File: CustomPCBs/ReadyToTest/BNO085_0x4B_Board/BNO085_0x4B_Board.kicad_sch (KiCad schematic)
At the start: 12 parts, among them J1 Conn_01x04_Pin, Y1 32.768kHz

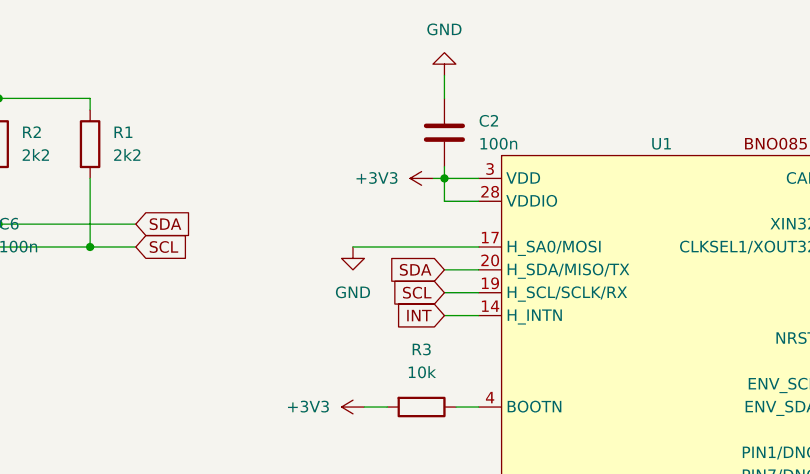
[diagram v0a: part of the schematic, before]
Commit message: Updating IMU boards for different wire connections
Now all components are placed on one layer, making assembly easier. The
JST connector was dropped for smalled IMU housing, instead the wires now
solder directly to the board and exit from the sides of the board.
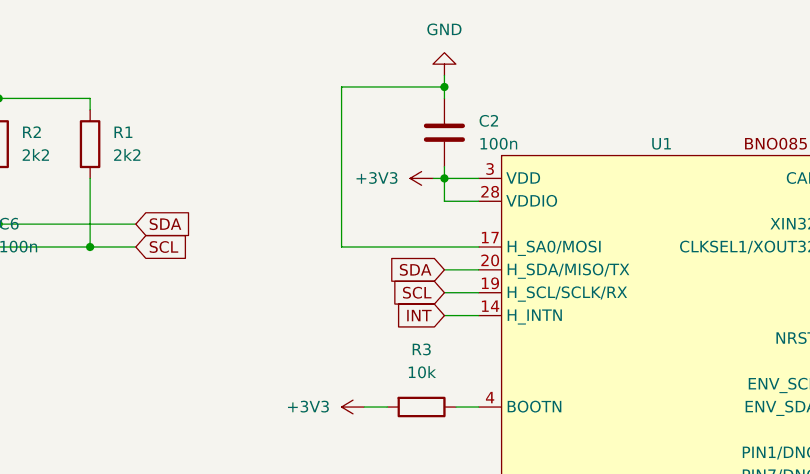
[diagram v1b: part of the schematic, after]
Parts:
- J1: footprint Connector_JST:JST_SH_SM04B-SRSS-TB_1x04-1MP_P1.00mm_Horizontal -> Library:WireToBoard2x2Wide
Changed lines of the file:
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@@
   (junction (at 40.64 38.1) (diameter 0) (color 0 0 0 0)
   )
+  (junction (at 90.17 22.86) (diameter 0) (color 0 0 0 0)
+  )
   (junction (at 173.99 40.64) (diameter 0) (color 0 0 0 0)
   )
@@
   (junction (at 158.75 40.64) (diameter 0) (color 0 0 0 0)
   )
-  (wire (pts (xy 80.01 40.64) (xy 93.98 40.64))
-    (stroke (width 0) (type default))
-  )
   (wire (pts (xy 90.17 73.66) (xy 93.98 73.66))
     (stroke (width 0) (type default))
@@
     (stroke (width 0) (type default))
   )
+  (wire (pts (xy 78.74 22.86) (xy 90.17 22.86))
+    (stroke (width 0) (type default))
+  )
   (wire (pts (xy 50.8 40.64) (xy 30.48 40.64))
     (stroke (width 0) (type default))
@@
     (stroke (width 0) (type default))
   )
+  (wire (pts (xy 78.74 40.64) (xy 93.98 40.64))
+    (stroke (width 0) (type default))
+  )
   (wire (pts (xy 173.99 40.64) (xy 173.99 41.91))
     (stroke (width 0) (type default))
   )
+  (wire (pts (xy 78.74 40.64) (xy 78.74 22.86))
+    (stroke (width 0) (type default))
+  )
   (wire (pts (xy 166.37 50.8) (xy 173.99 50.8))
     (stroke (width 0) (type default))
@@
     (stroke (width 0) (type default))
   )
+  (wire (pts (xy 90.17 22.86) (xy 90.17 24.13))
+    (stroke (width 0) (type default))
+  )
   (wire (pts (xy 90.17 81.28) (xy 90.17 83.82))
     (stroke (width 0) (type default))
@@
     (stroke (width 0) (type default))
   )
-  (wire (pts (xy 90.17 21.59) (xy 90.17 24.13))
+  (wire (pts (xy 90.17 21.59) (xy 90.17 22.86))
     (stroke (width 0) (type default))
   )
@@
     )
   )
-  (symbol (lib_id "power:GND") (at 80.01 40.64 0) (unit 1)
-    (in_bom yes) (on_board yes) (dnp no) (fields_autoplaced)
-    (property "Reference" "#PWR04" (at 80.01 46.99 0)
-      (effects (font (size 1.27 1.27)) hide)
-    )
-    (property "Value" "GND" (at 80.01 45.72 0)
-      (effects (font (size 1.27 1.27)))
-    )
-    (property "Footprint" "" (at 80.01 40.64 0)
-      (effects (font (size 1.27 1.27)) hide)
-    )
-    (property "Datasheet" "" (at 80.01 40.64 0)
-      (effects (font (size 1.27 1.27)) hide)
-    )
-    (pin "1")
-    (instances
-      (project "BNO085_0x4A_Board"
-        (path "/70e5a8fd-d79a-42f0-963c-2c04abcfaf88"
-          (reference "#PWR04") (unit 1)
-        )
-      )
-    )
-  )
   (symbol (lib_id "Device:R") (at 140.97 50.8 270) (unit 1)
     (in_bom yes) (on_board yes) (dnp no) (fields_autoplaced)
@@
     (pin "2")
     (instances
-      (project "BNO085_0x4A_Board"
+      (project "BNO085_0x4B_Board"
         (path "/70e5a8fd-d79a-42f0-963c-2c04abcfaf88"
           (reference "R4") (unit 1)
@@
     (pin "2")
     (instances
-      (project "BNO085_0x4A_Board"
+      (project "BNO085_0x4B_Board"
         (path "/70e5a8fd-d79a-42f0-963c-2c04abcfaf88"
           (reference "R1") (unit 1)
@@
     (pin "2")
     (instances
-      (project "BNO085_0x4A_Board"
+      (project "BNO085_0x4B_Board"
         (path "/70e5a8fd-d79a-42f0-963c-2c04abcfaf88"
           (reference "C6") (unit 1)
@@
     (pin "2")
     (instances
-      (project "BNO085_0x4A_Board"
+      (project "BNO085_0x4B_Board"
         (path "/70e5a8fd-d79a-42f0-963c-2c04abcfaf88"
           (reference "C1") (unit 1)
@@
     (pin "1")
     (instances
-      (project "BNO085_0x4A_Board"
+      (project "BNO085_0x4B_Board"
         (path "/70e5a8fd-d79a-42f0-963c-2c04abcfaf88"
           (reference "#PWR02") (unit 1)
@@
     (pin "1")
     (instances
-      (project "BNO085_0x4A_Board"
+      (project "BNO085_0x4B_Board"
         (path "/70e5a8fd-d79a-42f0-963c-2c04abcfaf88"
           (reference "#PWR011") (unit 1)
@@
     (pin "2")
     (instances
-      (project "BNO085_0x4A_Board"
+      (project "BNO085_0x4B_Board"
         (path "/70e5a8fd-d79a-42f0-963c-2c04abcfaf88"
           (reference "C5") (unit 1)
@@
       (effects (font (size 1.27 1.27)))
     )
-    (property "Footprint" "Connector_JST:JST_SH_SM04B-SRSS-TB_1x04-1MP_P1.00mm_Horizontal" (at 25.4 38.1 0)
+    (property "Footprint" "Library:WireToBoard2x2Wide" (at 25.4 38.1 0)
       (effects (font (size 1.27 1.27)) hide)
     )
@@
     (pin "4")
     (instances
-      (project "BNO085_0x4A_Board"
+      (project "BNO085_0x4B_Board"
         (path "/70e5a8fd-d79a-42f0-963c-2c04abcfaf88"
           (reference "J1") (unit 1)
@@
     (pin "9")
     (instances
-      (project "BNO085_0x4A_Board"
+      (project "BNO085_0x4B_Board"
         (path "/70e5a8fd-d79a-42f0-963c-2c04abcfaf88"
           (reference "U1") (unit 1)
@@
     (pin "1")
     (instances
-      (project "BNO085_0x4A_Board"
+      (project "BNO085_0x4B_Board"
         (path "/70e5a8fd-d79a-42f0-963c-2c04abcfaf88"
           (reference "#PWR06") (unit 1)
@@
     (pin "1")
     (instances
-      (project "BNO085_0x4A_Board"
+      (project "BNO085_0x4B_Board"
         (path "/70e5a8fd-d79a-42f0-963c-2c04abcfaf88"
           (reference "#PWR08") (unit 1)
@@
     (pin "2")
     (instances
-      (project "BNO085_0x4A_Board"
+      (project "BNO085_0x4B_Board"
         (path "/70e5a8fd-d79a-42f0-963c-2c04abcfaf88"
           (reference "C4") (unit 1)
@@
     (pin "2")
     (instances
-      (project "BNO085_0x4A_Board"
+      (project "BNO085_0x4B_Board"
         (path "/70e5a8fd-d79a-42f0-963c-2c04abcfaf88"
           (reference "Y1") (unit 1)
@@
     (pin "1")
     (instances
-      (project "BNO085_0x4A_Board"
+      (project "BNO085_0x4B_Board"
         (path "/70e5a8fd-d79a-42f0-963c-2c04abcfaf88"
           (reference "#PWR03") (unit 1)
@@
     (pin "1")
     (instances
-      (project "BNO085_0x4A_Board"
+      (project "BNO085_0x4B_Board"
         (path "/70e5a8fd-d79a-42f0-963c-2c04abcfaf88"
           (reference "#PWR010") (unit 1)
@@
     (pin "2")
     (instances
-      (project "BNO085_0x4A_Board"
+      (project "BNO085_0x4B_Board"
         (path "/70e5a8fd-d79a-42f0-963c-2c04abcfaf88"
           (reference "C2") (unit 1)
@@
     (pin "1")
     (instances
-      (project "BNO085_0x4A_Board"
+      (project "BNO085_0x4B_Board"
         (path "/70e5a8fd-d79a-42f0-963c-2c04abcfaf88"
           (reference "#PWR01") (unit 1)
@@
     (pin "1")
     (instances
-      (project "BNO085_0x4A_Board"
+      (project "BNO085_0x4B_Board"
         (path "/70e5a8fd-d79a-42f0-963c-2c04abcfaf88"
           (reference "#PWR09") (unit 1)
@@
     (pin "2")
     (instances
-      (project "BNO085_0x4A_Board"
+      (project "BNO085_0x4B_Board"
         (path "/70e5a8fd-d79a-42f0-963c-2c04abcfaf88"
           (reference "R3") (unit 1)
@@
     (pin "2")
     (instances
-      (project "BNO085_0x4A_Board"
+      (project "BNO085_0x4B_Board"
         (path "/70e5a8fd-d79a-42f0-963c-2c04abcfaf88"
           (reference "R2") (unit 1)
@@
     (pin "1")
     (instances
-      (project "BNO085_0x4A_Board"
+      (project "BNO085_0x4B_Board"
         (path "/70e5a8fd-d79a-42f0-963c-2c04abcfaf88"
           (reference "#PWR012") (unit 1)
